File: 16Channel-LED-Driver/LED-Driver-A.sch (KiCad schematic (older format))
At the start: 42 parts, among them P6 CONN_01X08, Q10 BC413, Q11 BUT11, Q12 BC413, Q13 BUT11, Q2 BC413, Q3 BC413, Q4 BC413, Q5 BUT11, Q6 BC413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

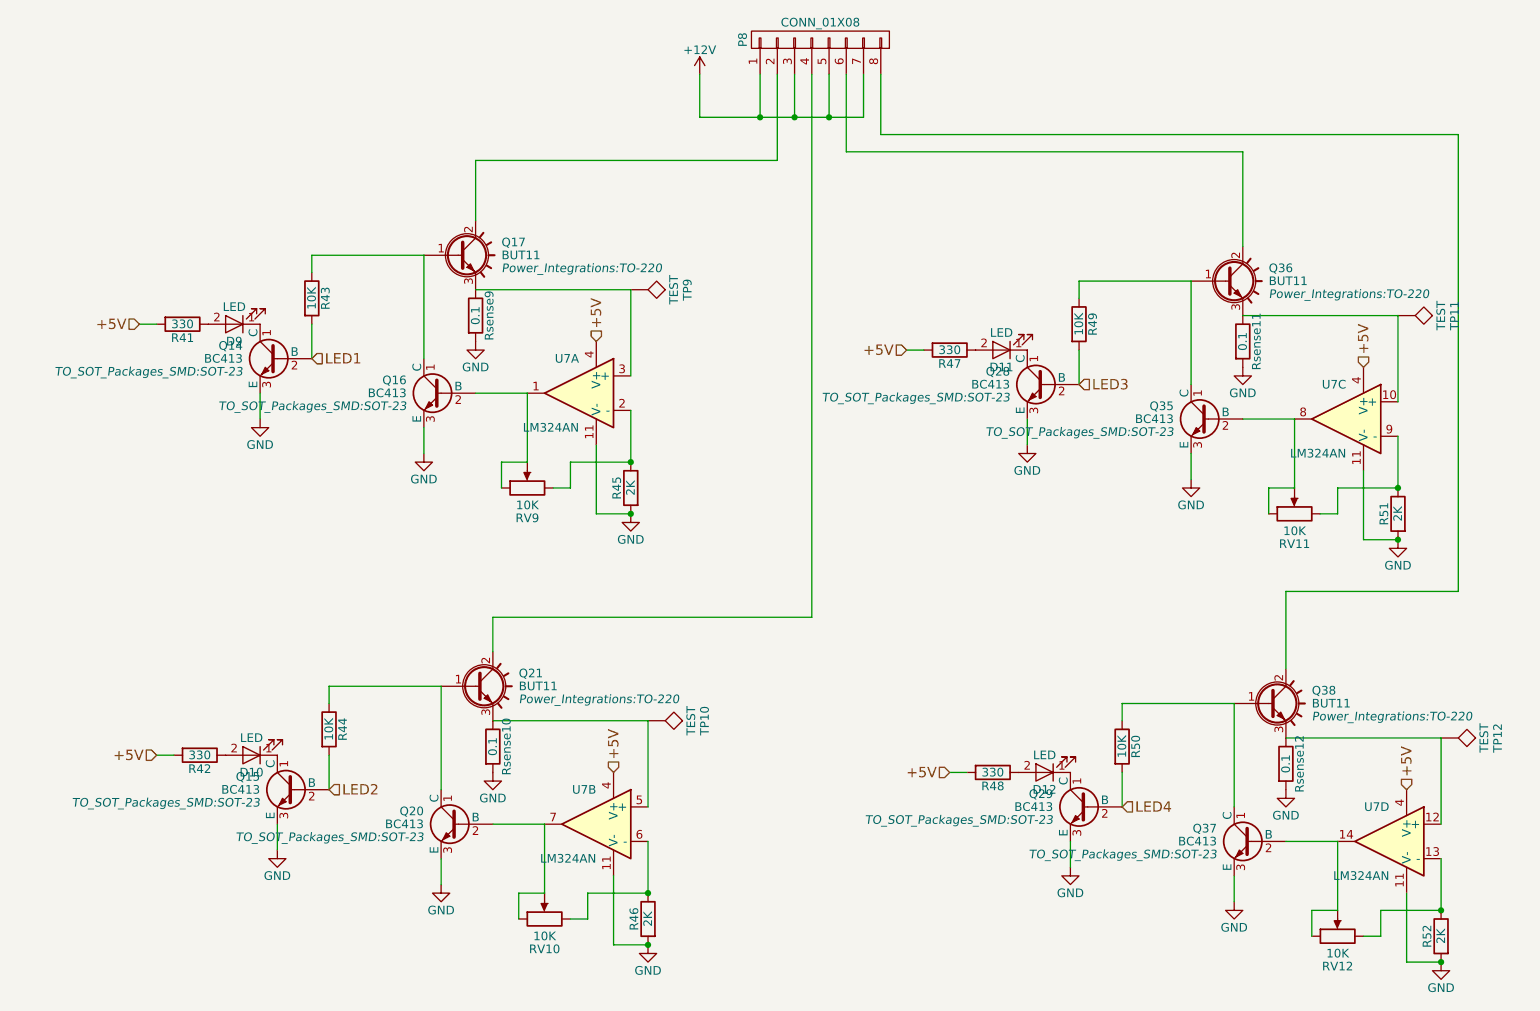
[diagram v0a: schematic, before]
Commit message: Did Revision B of the 16 Channel board, also exported some gerbers
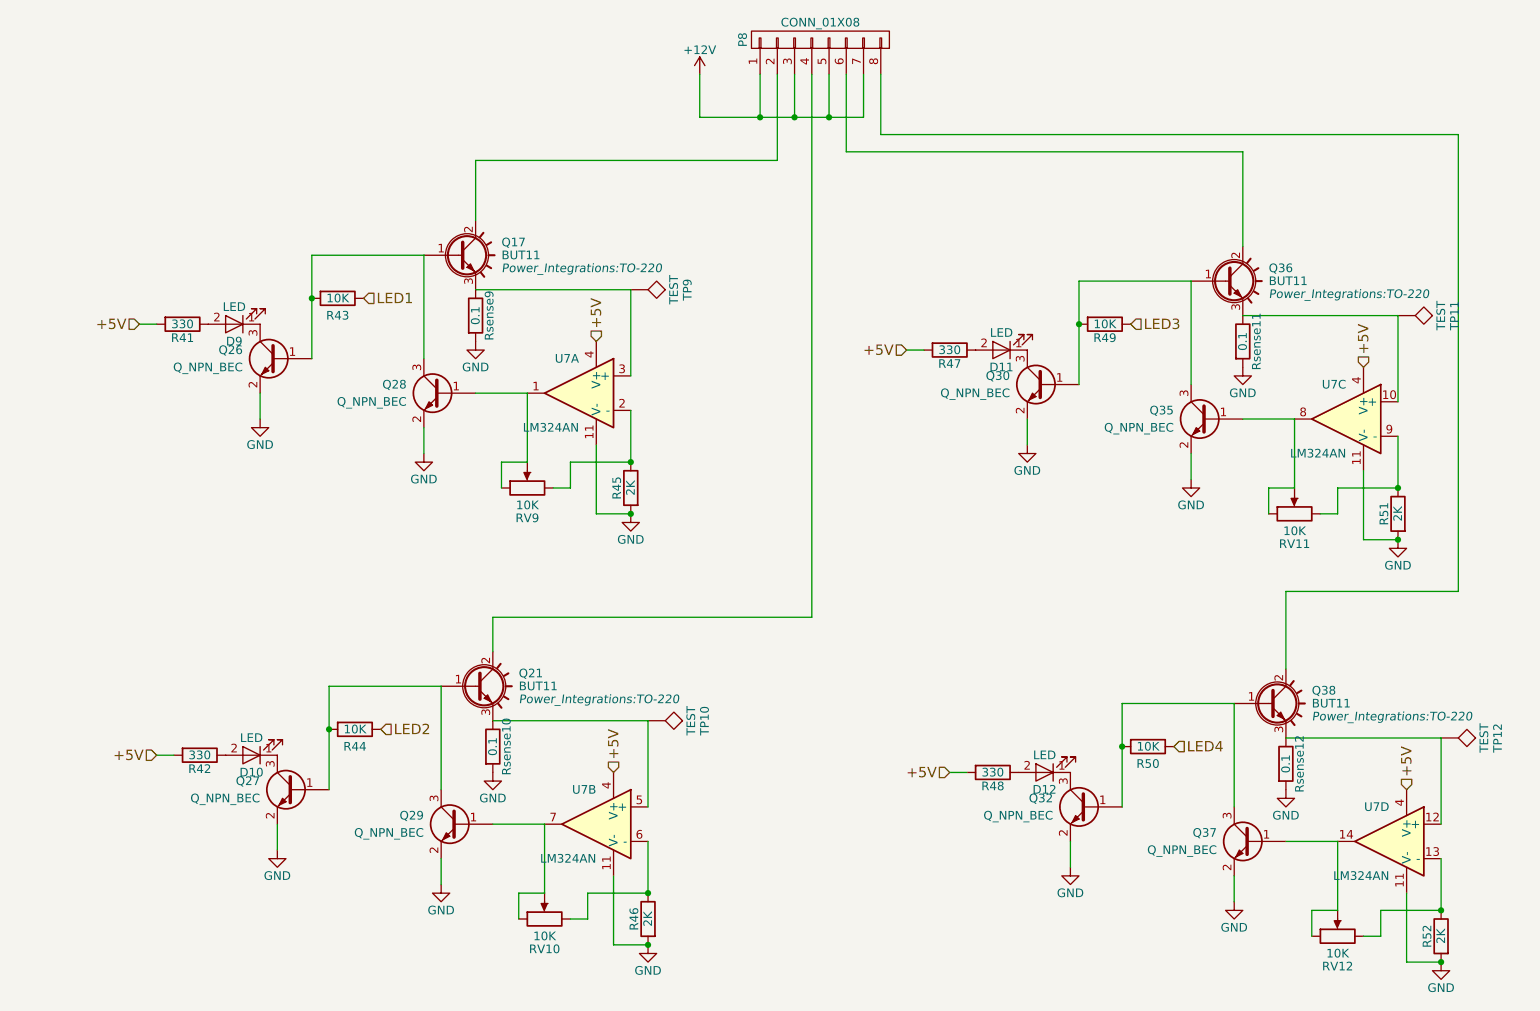
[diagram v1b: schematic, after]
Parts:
- removed Q10, Q12, Q2, Q3, Q4, Q6, Q8, Q9: BC413, TO_SOT_Packages_SMD:SOT-23, symbol BC413
- added Q10, Q12, Q2, Q3, Q4, Q6, Q8, Q9: Q_NPN_BEC, TO_SOT_Packages_SMD:SOT-23, symbol Q_NPN_BEC
- Rsense1, Rsense2, Rsense3, Rsense4: footprint Custom_Footprints:Current_Sense_Resistor -> Resistors_SMD:R_1206_HandSoldering
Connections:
- net GND: now also Q10.2 (E), Q12.2 (E), Q2.2 (E), Q3.2 (E), Q4.2 (E), Q6.2 (E), Q8.2 (E), Q9.2 (E)
- net LED1: now also R11.1; no longer R11.2
- net LED2: now also R12.1; no longer R12.2
- net LED3: now also R17.1; no longer R17.2
- net LED4: now also R18.1; no longer R18.2
- net at RV1.1, RV1.2, U4.1: now also Q4.1 (B)
- net at Q5.1 (B): now also R11.2, Q2.1 (B), Q4.3 (C); no longer R11.1
- net at D1.1 (K): now also Q2.3 (C)
- net at RV3.1, RV3.2, U4.8: now also Q10.1 (B)
- net at Q11.1 (B): now also R17.2, Q10.3 (C), Q8.1 (B); no longer R17.1
- net at D3.1 (K): now also Q8.3 (C)
- net at RV2.1, RV2.2, U4.7: now also Q6.1 (B)
- net at RV4.1, RV4.2, U4.14: now also Q12.1 (B)
- net at Q13.1 (B): now also R18.2, Q12.3 (C), Q9.1 (B); no longer R18.1
- net at Q7.1 (B): now also R12.2, Q3.1 (B), Q6.3 (C); no longer R12.1
- net at D2.1 (K): now also Q3.3 (C)
- net at D4.1 (K): now also Q9.3 (C)
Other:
- moved on the sheet: R43, R44, R49, R50

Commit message: Did third and hopefully final revision of the 16 channel LED board. I like making dumb mistakes. :(
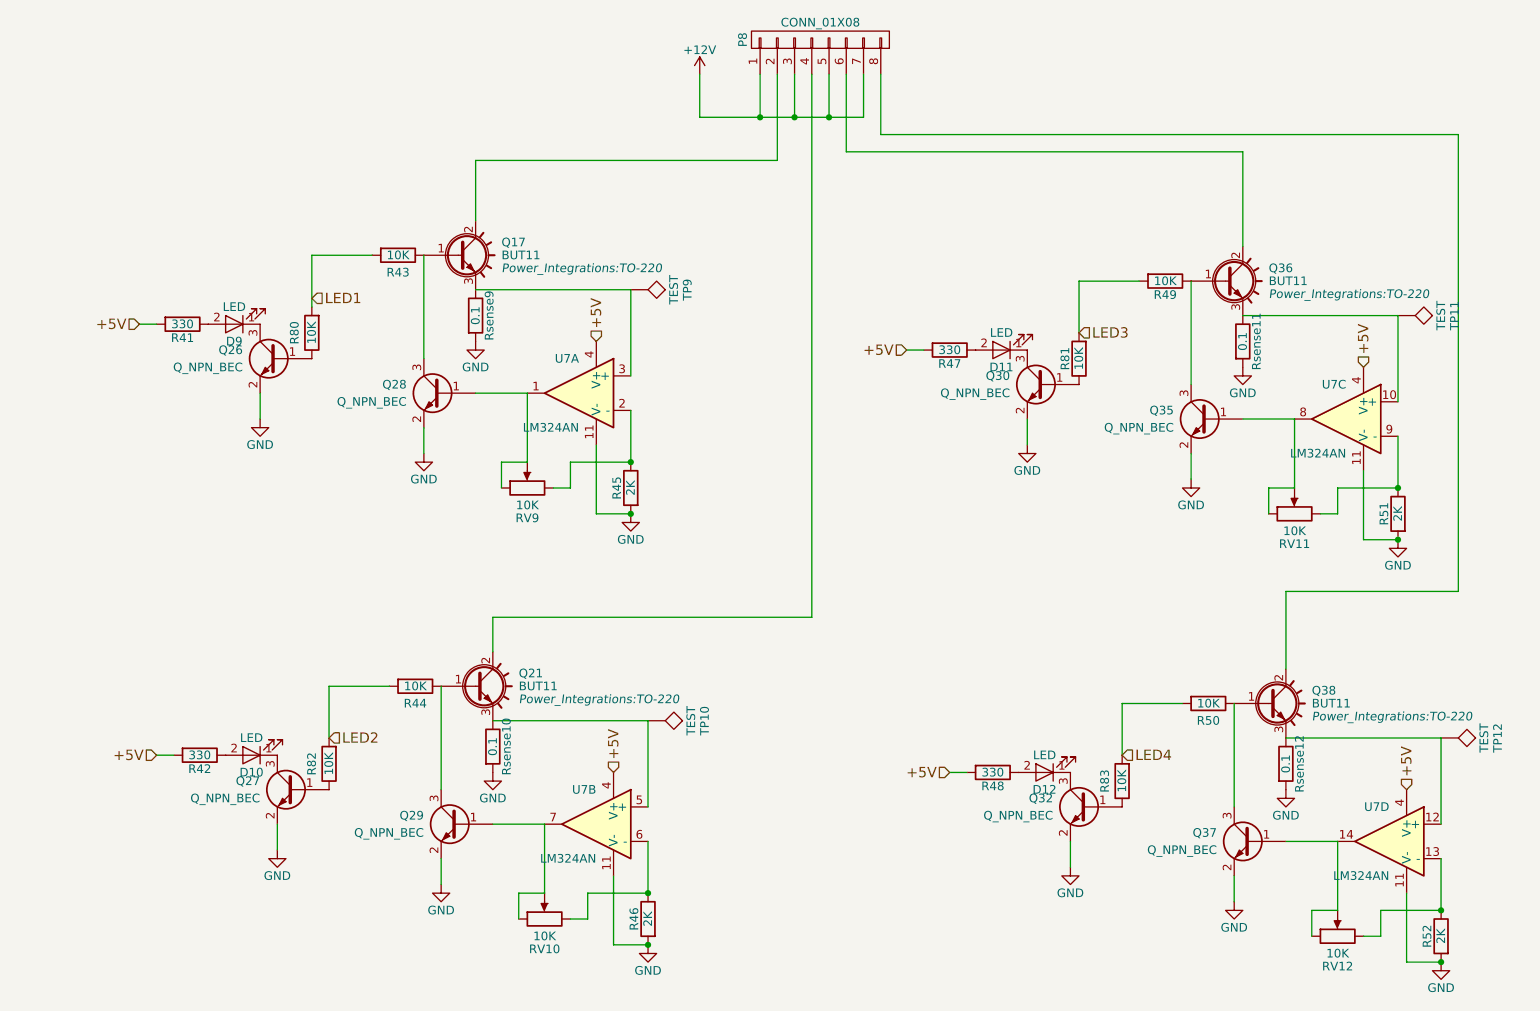
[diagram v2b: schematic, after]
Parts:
- added R76, R77, R78, R79: 10K, Resistors_SMD:R_0805_HandSoldering, symbol R
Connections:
- net LED1: now also R11.2, R76.2; no longer R11.1
- net LED2: now also R12.2, R78.2; no longer R12.1
- net LED3: now also R17.2, R77.2; no longer R17.1
- net LED4: now also R18.2, R79.2; no longer R18.1
- net at Q4.3 (C), Q5.1 (B): now also R11.1; no longer Q2.1 (B), R11.2
- net at Q10.3 (C), Q11.1 (B): now also R17.1; no longer Q8.1 (B), R17.2
- net at Q12.3 (C), Q13.1 (B): now also R18.1; no longer Q9.1 (B), R18.2
- net at Q6.3 (C), Q7.1 (B): now also R12.1; no longer Q3.1 (B), R12.2
- new net: Q2.1 (B), R76.1
- new net: Q3.1 (B), R78.1
- new net: Q9.1 (B), R79.1
- new net: Q8.1 (B), R77.1
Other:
- moved on the sheet: R43, R44, R49, R50

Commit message: Rev D of the 16 Channel board. Fixed an issue with the opamp driving BJTs
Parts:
- added R84, R85, R86, R87: 10K, Resistors_SMD:R_0805_HandSoldering, symbol R
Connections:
- net at RV1.1, RV1.2, U4.1: now also R84.1; no longer Q4.1 (B)
- net at RV3.1, RV3.2, U4.8: now also R86.1; no longer Q10.1 (B)
- net at RV2.1, RV2.2, U4.7: now also R85.1; no longer Q6.1 (B)
- net at RV4.1, RV4.2, U4.14: now also R87.1; no longer Q12.1 (B)
- new net: Q4.1 (B), R84.2
- new net: Q6.1 (B), R85.2
- new net: Q12.1 (B), R87.2
- new net: Q10.1 (B), R86.2
